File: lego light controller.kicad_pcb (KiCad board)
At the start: 2 copper layers, 31.8 x 31.8 mm, 29 parts, among them J1 Conn_01x02, J2 Conn_01x02, J3 Conn_01x02, J4 Conn_01x03, J5 Conn_01x03, J7 Conn_01x06_Pin, P1 USB_C_Plug_USB2.0, Q1 BC847W, Q2 BC847W, Q3 BC847W, U1 ATSAMD11C14A-SS, U2 AMS1117-3.3

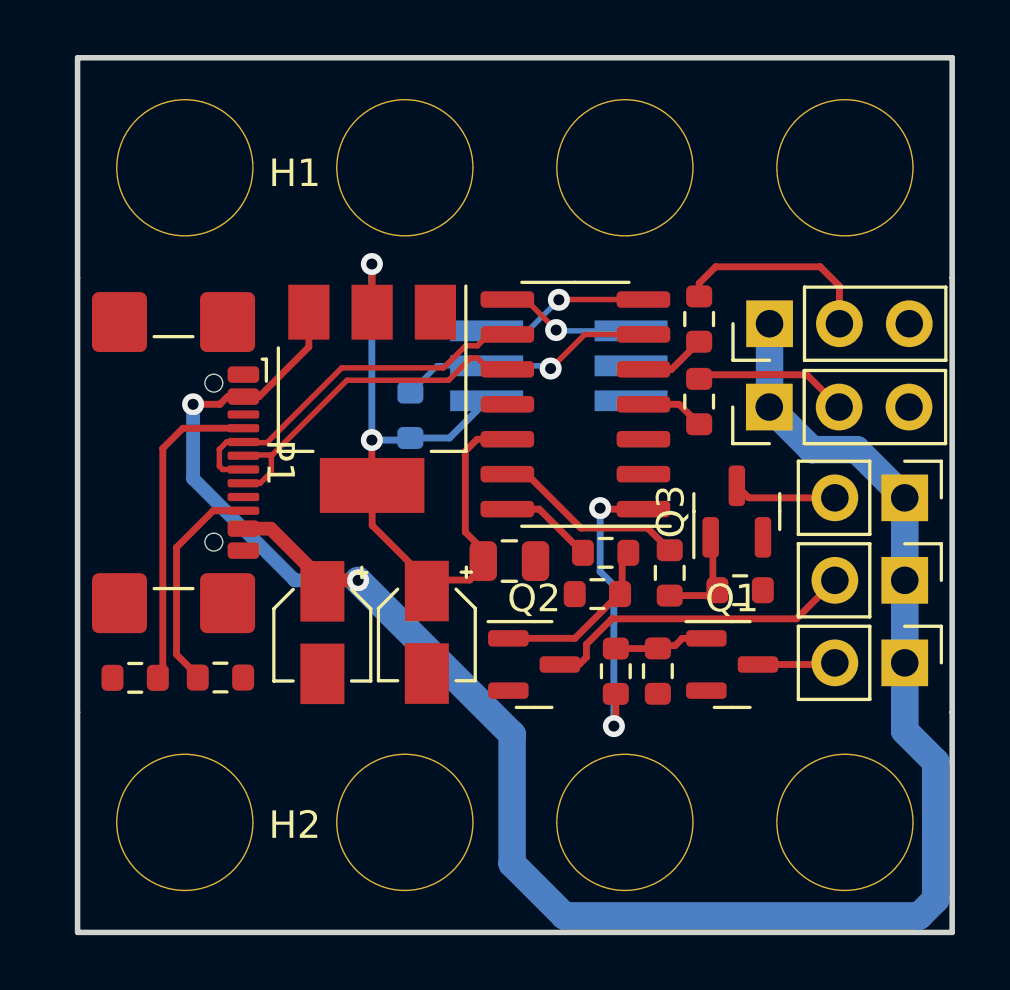
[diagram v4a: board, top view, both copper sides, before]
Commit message: move usb to center
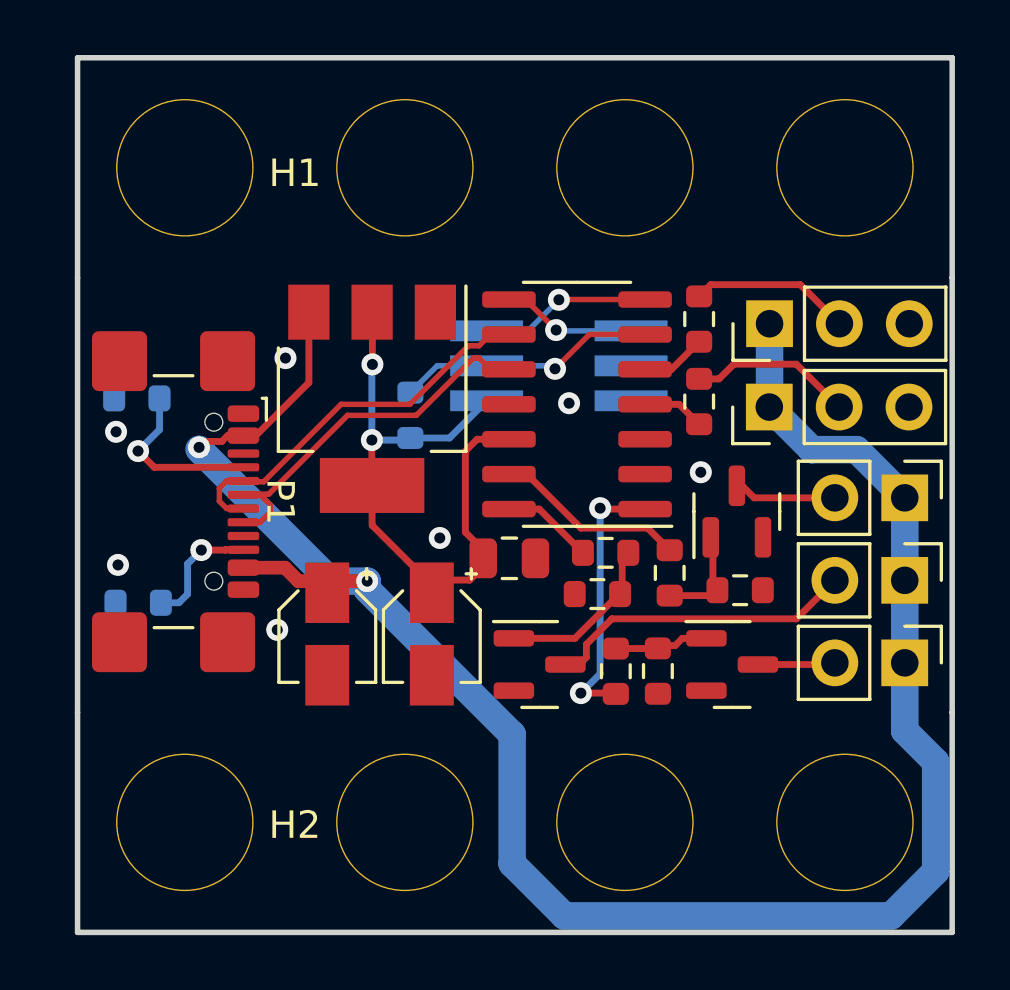
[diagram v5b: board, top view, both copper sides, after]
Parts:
- R1, R2: moved to B.Cu
- moved R1 10.2 mm to (182.2, 84.4)
- moved G*** 7.77 mm to (184.2, 88.2)
- moved R2 4.04 mm to (182.2, 91.8), turned to 180 degrees
- moved P1 1.42 mm to (182.3, 88.1)
- moved Q2 0.20 mm to (196.8, 94.1)
- moved C2 0.19 mm to (192.9, 93.0)
- moved C1 0.19 mm to (189.1, 93.0)
- moved C3 0.10 mm to (195.7, 90.2)
- moved U1 0.06 mm to (198.2, 84.6)
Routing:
- net Net-(P1-CC1): track 11.7 -> 6.31 mm, vias 0 -> 1
- net Net-(P1-CC2): track 8.03 -> 4.44 mm, vias 0 -> 1
- net +3V3: track 27.5 -> 24.0 mm
- net /USB_P: track 13.0 -> 15.1 mm
- net +5V: track 75.0 -> 73.0 mm
- net Net-(J5-Pin_2): track 7.48 -> 5.86 mm
- net /USB_N: track 13.8 -> 15.0 mm
- net /LED3: track 10.9 -> 9.89 mm
- net GND: vias 0 -> 7

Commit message: add pads to unused io
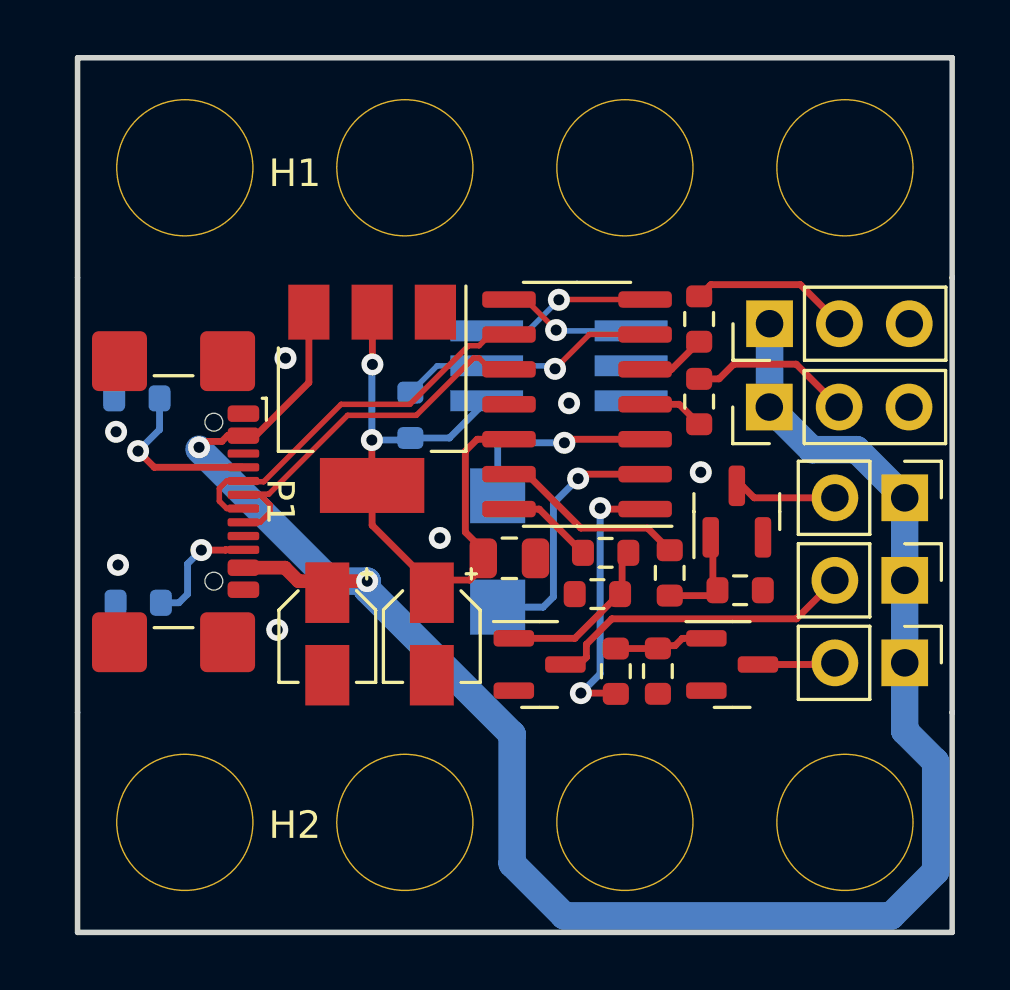
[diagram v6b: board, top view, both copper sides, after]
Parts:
- added TP1: TestPoint, TestPoint:TestPoint_Pad_2.0x2.0mm, B.Cu at (195.3, 92.0)
- added TP2: TestPoint, TestPoint:TestPoint_Pad_2.0x2.0mm, B.Cu at (195.3, 87.9)
- U2: value AMS1117-3.3 -> AP2111H-3.3TRG1
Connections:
- U1 pad 2: unconnected-(U1-PA08/XIN-Pad2) -> /EXT1
- U1 pad 3: unconnected-(U1-PA09/XOUT-Pad3) -> /EXT2
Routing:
- net /EXT1: track 0.00 -> 9.35 mm, vias 0 -> 1
- net /EXT2: track 0.00 -> 7.27 mm, vias 0 -> 1
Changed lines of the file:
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@@
   (net 17 "/DL1")
   (net 18 "/DL2")
-  (net 19 "unconnected-(U1-PA08{slash}XIN-Pad2)")
-  (net 20 "unconnected-(U1-PA09{slash}XOUT-Pad3)")
+  (net 19 "/EXT1")
+  (net 20 "/EXT2")
   (net 21 "Net-(J7-Pin_2)")
   (net 22 "Net-(J7-Pin_3)")
@@
     (property "ki_keywords" "cap capacitor")
     (attr smd)
-    (fp_text reference "C1" (at 0.24 -0.1 90) (layer "B.SilkS")
+    (fp_text reference "C1" (at -0.96 -0.2 90) (layer "B.SilkS")
         (effects (font (size 1 1) (thickness 0.15)) (justify mirror))
     )
@@
       (net 14 "/LED3") (pinfunction "PA05") (pintype "bidirectional"))
     (pad "2" smd roundrect (at -2.475 -2.54 180) (size 1.95 0.6) (layers "F.Cu" "F.Paste" "F.Mask") (roundrect_rratio 0.25)
-      (net 19 "unconnected-(U1-PA08{slash}XIN-Pad2)") (pinfunction "PA08/XIN") (pintype "bidirectional+no_connect"))
+      (net 19 "/EXT1") (pinfunction "PA08/XIN") (pintype "bidirectional"))
     (pad "3" smd roundrect (at -2.475 -1.27 180) (size 1.95 0.6) (layers "F.Cu" "F.Paste" "F.Mask") (roundrect_rratio 0.25)
-      (net 20 "unconnected-(U1-PA09{slash}XOUT-Pad3)") (pinfunction "PA09/XOUT") (pintype "bidirectional+no_connect"))
+      (net 20 "/EXT2") (pinfunction "PA09/XOUT") (pintype "bidirectional"))
     (pad "4" smd roundrect (at -2.475 0 180) (size 1.95 0.6) (layers "F.Cu" "F.Paste" "F.Mask") (roundrect_rratio 0.25)
       (net 17 "/DL1") (pinfunction "PA14") (pintype "bidirectional"))
@@
     (property "ki_keywords" "cap capacitor")
     (attr smd)
-    (fp_text reference "C3" (at 0.08 0.24 90) (layer "B.SilkS")
+    (fp_text reference "C3" (at -1.52 -0.06 90) (layer "B.SilkS")
         (effects (font (size 1 1) (thickness 0.15)) (justify mirror))
     )
@@
     (property "ki_keywords" "NPN Small Signal Transistor")
     (attr smd)
-    (fp_text reference "Q2" (at -0.15 -0.06 -90) (layer "B.SilkS")
+    (fp_text reference "Q2" (at 0.35 -0.06 -90) (layer "B.SilkS")
         (effects (font (size 1 1) (thickness 0.15)) (justify mirror))
     )
@@
     (descr "module CMS SOT223 4 pins")
     (tags "CMS SOT")
-    (property "MPN" "AMS1117-3.3")
+    (property "MPN" "AP2111H-3.3TRG1")
     (property "Sheetfile" "lego light controller.kicad_sch")
     (property "Sheetname" "")
@@
         (effects (font (size 1 1) (thickness 0.15)) (justify mirror))
     )
-    (fp_text value "AMS1117-3.3" (at 0 4.5 90) (layer "F.Fab")
+    (fp_text value "AP2111H-3.3TRG1" (at 0 4.5 90) (layer "F.Fab")
         (effects (font (size 1 1) (thickness 0.15)))
     )
@@
     (property "ki_keywords" "cap capacitor")
     (attr smd)
-    (fp_text reference "C2" (at 0.32 -0.11 90) (layer "B.SilkS")
+    (fp_text reference "C2" (at -0.98 0.99 90) (layer "B.SilkS")
         (effects (font (size 1 1) (thickness 0.15)) (justify mirror))
     )
@@
     )
   )
+  (footprint "TestPoint:TestPoint_Pad_2.0x2.0mm" (layer "B.Cu")
+    (at 195.275 91.975)
+    (descr "SMD rectangular pad as test Point, square 2.0mm side length")
+    (tags "test point SMD pad rectangle square")
+    (property "Sheetfile" "lego light controller.kicad_sch")
+    (property "Sheetname" "")
+    (property "ki_description" "test point")
+    (property "ki_keywords" "test point tp")
+    (attr exclude_from_pos_files)
+    (fp_text reference "TP1" (at -1.902 -0.05 90) (layer "B.SilkS")
+        (effects (font (size 1 1) (thickness 0.15)) (justify mirror))
+    )
+    (fp_text value "TestPoint" (at 0 -2.05) (layer "B.Fab")
+        (effects (font (size 1 1) (thickness 0.15)) (justify mirror))
+    )
+    (fp_text user "${REFERENCE}" (at 0 2) (layer "B.Fab")
+        (effects (font (size 1 1) (thickness 0.15)) (justify mirror))
+    )
+    (fp_line (start -1.2 -1.2) (end -1.2 1.2)
+      (stroke (width 0.12) (type solid)) (layer "B.SilkS"))
+    (fp_line (start -1.2 1.2) (end 1.2 1.2)
+      (stroke (width 0.12) (type solid)) (layer "B.SilkS"))
+    (fp_line (start 1.2 -1.2) (end -1.2 -1.2)
+      (stroke (width 0.12) (type solid)) (layer "B.SilkS"))
+    (fp_line (start 1.2 1.2) (end 1.2 -1.2)
+      (stroke (width 0.12) (type solid)) (layer "B.SilkS"))
+    (fp_line (start -1.5 1.5) (end -1.5 -1.5)
+      (stroke (width 0.05) (type solid)) (layer "B.CrtYd"))
+    (fp_line (start -1.5 1.5) (end 1.5 1.5)
+      (stroke (width 0.05) (type solid)) (layer "B.CrtYd"))
+    (fp_line (start 1.5 -1.5) (end -1.5 -1.5)
+      (stroke (width 0.05) (type solid)) (layer "B.CrtYd"))
+    (fp_line (start 1.5 -1.5) (end 1.5 1.5)
+      (stroke (width 0.05) (type solid)) (layer "B.CrtYd"))
+    (pad "1" smd rect (at 0 0) (size 2 2) (layers "B.Cu" "B.Mask")
+      (net 19 "/EXT1") (pinfunction "1") (pintype "passive"))
+  )
   (footprint "Resistor_SMD:R_0603_1608Metric" (layer "B.Cu")
     (at 182.155 84.385 180)
@@
     )
   )
+  (footprint "TestPoint:TestPoint_Pad_2.0x2.0mm" (layer "B.Cu")
+    (at 195.275 87.925)
+    (descr "SMD rectangular pad as test Point, square 2.0mm side length")
+    (tags "test point SMD pad rectangle square")
+    (property "Sheetfile" "lego light controller.kicad_sch")
+    (property "Sheetname" "")
+    (property "ki_description" "test point")
+    (property "ki_keywords" "test point tp")
+    (attr exclude_from_pos_files)
+    (fp_text reference "TP2" (at -1.852 0 90) (layer "B.SilkS")
+        (effects (font (size 1 1) (thickness 0.15)) (justify mirror))
+    )
+    (fp_text value "TestPoint" (at 0 -2.05) (layer "B.Fab")
+        (effects (font (size 1 1) (thickness 0.15)) (justify mirror))
+    )
+    (fp_text user "${REFERENCE}" (at 0 2) (layer "B.Fab")
+        (effects (font (size 1 1) (thickness 0.15)) (justify mirror))
+    )
+    (fp_line (start -1.2 -1.2) (end -1.2 1.2)
+      (stroke (width 0.12) (type solid)) (layer "B.SilkS"))
+    (fp_line (start -1.2 1.2) (end 1.2 1.2)
+      (stroke (width 0.12) (type solid)) (layer "B.SilkS"))
+    (fp_line (start 1.2 -1.2) (end -1.2 -1.2)
+      (stroke (width 0.12) (type solid)) (layer "B.SilkS"))
+    (fp_line (start 1.2 1.2) (end 1.2 -1.2)
+      (stroke (width 0.12) (type solid)) (layer "B.SilkS"))
+    (fp_line (start -1.5 1.5) (end -1.5 -1.5)
+      (stroke (width 0.05) (type solid)) (layer "B.CrtYd"))
+    (fp_line (start -1.5 1.5) (end 1.5 1.5)
+      (stroke (width 0.05) (type solid)) (layer "B.CrtYd"))
+    (fp_line (start 1.5 -1.5) (end -1.5 -1.5)
+      (stroke (width 0.05) (type solid)) (layer "B.CrtYd"))
+    (fp_line (start 1.5 -1.5) (end 1.5 1.5)
+      (stroke (width 0.05) (type solid)) (layer "B.CrtYd"))
+    (pad "1" smd rect (at 0 0) (size 2 2) (layers "B.Cu" "B.Mask")
+      (net 20 "/EXT2") (pinfunction "1") (pintype "passive"))
+  )
   (footprint "Custom:bee logo small" (layer "B.Cu")
     (at 184.24 88.15 -90)
@@
   (segment (start 200.575 83.33) (end 201.595 83.33) (width 0.25) (layer "F.Cu") (net 18))
   (segment (start 201.595 83.33) (end 202.6 82.325) (width 0.25) (layer "F.Cu") (net 18))
+  (segment (start 198.36 87.14) (end 198.2 87.3) (width 0.25) (layer "F.Cu") (net 19))
+  (segment (start 200.635 87.14) (end 198.36 87.14) (width 0.25) (layer "F.Cu") (net 19))
+  (via (at 198.2 87.3) (size 0.8) (drill 0.4) (layers "F.Cu" "B.Cu") (net 19))
+  (segment (start 196.925 91.975) (end 195.275 91.975) (width 0.25) (layer "B.Cu") (net 19))
+  (segment (start 197.3 88.2) (end 197.3 91.6) (width 0.25) (layer "B.Cu") (net 19))
+  (segment (start 197.3 91.6) (end 196.925 91.975) (width 0.25) (layer "B.Cu") (net 19))
+  (segment (start 198.2 87.3) (end 197.3 88.2) (width 0.25) (layer "B.Cu") (net 19))
+  (segment (start 197.83 85.87) (end 197.7 86) (width 0.25) (layer "F.Cu") (net 20))
+  (segment (start 200.635 85.87) (end 197.83 85.87) (width 0.25) (layer "F.Cu") (net 20))
+  (via (at 197.7 86) (size 0.8) (drill 0.4) (layers "F.Cu" "B.Cu") (net 20))
+  (segment (start 195.275 86.125) (end 195.275 87.925) (width 0.25) (layer "B.Cu") (net 20))
+  (segment (start 197.7 86) (end 195.4 86) (width 0.25) (layer "B.Cu") (net 20))
+  (segment (start 195.4 86) (end 195.275 86.125) (width 0.25) (layer "B.Cu") (net 20))
   (segment (start 197.36 83.31) (end 198.61 82.06) (width 0.2) (layer "F.Cu") (net 21))
   (segment (start 198.61 82.06) (end 200.575 82.06) (width 0.2) (layer "F.Cu") (net 21))
